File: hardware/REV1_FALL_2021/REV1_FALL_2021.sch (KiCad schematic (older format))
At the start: 23 parts, among them J101 Screw_Terminal_01x02, Q101 Q_NMOS_GDS, U1 Teensy3.6_All_Pins, U2 PA16165_Breakout, U3 MPL3115A2_Breakout, U4 BNO055_Breakout, U5 RFM69HCW_Breakout

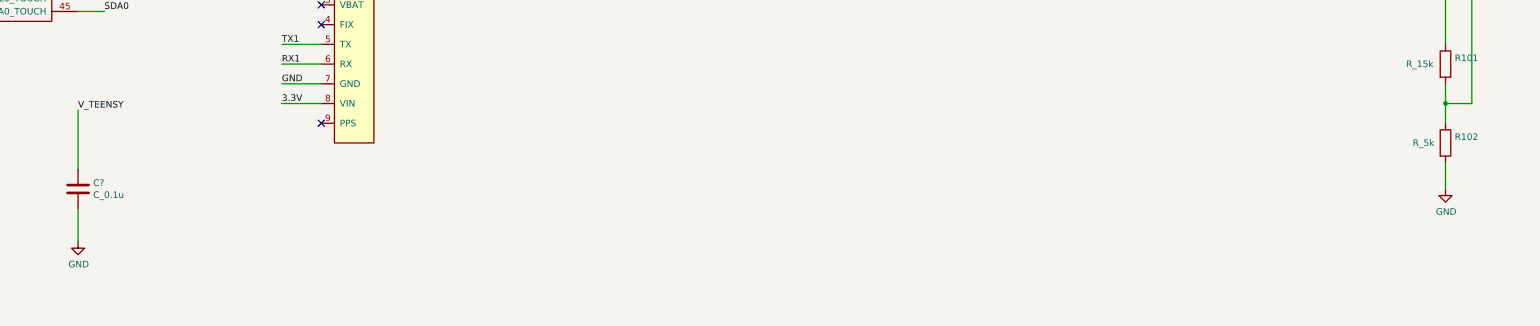
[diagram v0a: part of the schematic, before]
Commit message: change resistance of one voltage divider resistor
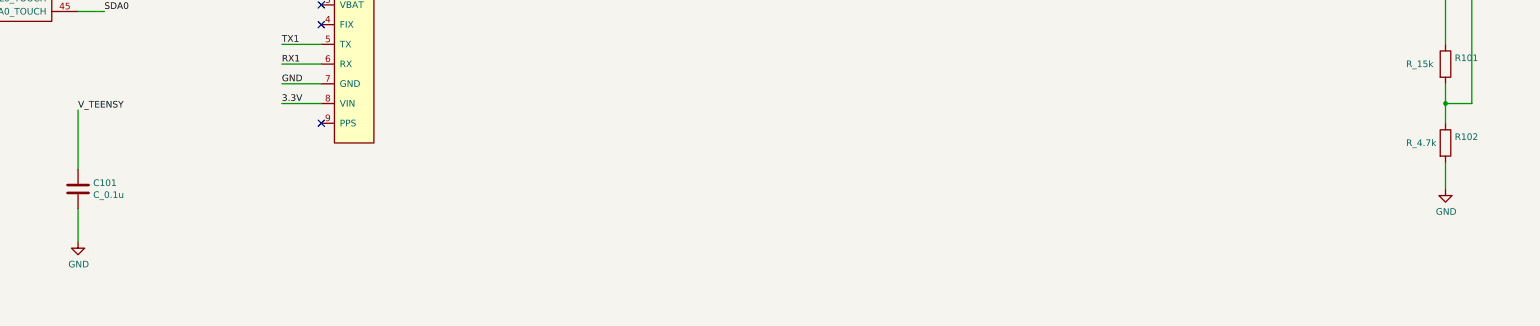
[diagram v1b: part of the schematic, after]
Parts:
- R102: value R_5k -> R_4.7k
- gave numbers to parts that had none: 1
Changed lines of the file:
@@
 P 14150 6750
 F 0 "R102" H 14220 6796 50  0000 L CNN
-F 1 "R_5k" H 13900 6750 50  0000 L CNN
+F 1 "R_4.7k" H 13850 6750 50  0000 L CNN
 F 2 "Resistor_SMD:R_0805_2012Metric_Pad1.20x1.40mm_HandSolder" V 14080 6750 50  0001 C CNN
 F 3 "~" H 14150 6750 50  0001 C CNN
@@
 3.3V
 $Comp
-L Device:C C?
+L Device:C C101
 U 1 1 61A04C38
 P 3750 7100
-F 0 "C?" H 3865 7146 50  0000 L CNN
+F 0 "C101" H 3865 7146 50  0000 L CNN
 F 1 "C_0.1u" H 3865 7055 50  0000 L CNN
 F 2 "Capacitor_SMD:C_0805_2012Metric_Pad1.18x1.45mm_HandSolder" H 3788 6950 50  0001 C CNN
@@
 $EndComp
 $Comp
-L power:GND #PWR?
+L power:GND #PWR0107
 U 1 1 61A05A03
 P 3750 7500
-F 0 "#PWR?" H 3750 7250 50  0001 C CNN
+F 0 "#PWR0107" H 3750 7250 50  0001 C CNN
 F 1 "GND" H 3755 7327 50  0000 C CNN
 F 2 "" H 3750 7500 50  0001 C CNN

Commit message: Add second e-match
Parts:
- added J102: Screw_Terminal_01x02, TerminalBlock:TerminalBlock_bornier-2_P5.08mm, symbol Connector:Screw_Terminal_01x02
- added Q102: Q_NMOS_GDS, footprints:TO-220-3, symbol Device:Q_NMOS_GDS
- added R109: R_10k, Resistor_SMD:R_0805_2012Metric_Pad1.20x1.40mm_HandSolder, symbol Device:R
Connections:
- net GND: now also Q102.3 (S)
- net V_EMATCH: now also J102.1 (Pin_1)
- net E-MATCH_TRIGGER_1: now reaches U1.35 (38_A19_PWM_SDA1)
- net E-MATCH_TRIGGER_1: now also R103.2
- net E-MATCH_TRIGGER renamed E-MATCH_TRIGGER_2
- net E-MATCH_TRIGGER_2: now also R109.2; no longer R103.2
- new net: J102.2 (Pin_2), Q102.2 (D)
- new net: Q102.1 (G), R109.1
- no-connect marks 85 -> 84
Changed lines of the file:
@@
 NoConn ~ 1450 4350
 NoConn ~ 1450 4450
-NoConn ~ 1450 4850
 NoConn ~ 1450 5050
 NoConn ~ 1450 5150
@@
 Text Label 4250 4950 0    50   ~ 0
 V_TEENSY
-Text Label 1350 4950 2    50   ~ 0
-E-MATCH_TRIGGER
+Text Label 1350 4850 2    50   ~ 0
+E-MATCH_TRIGGER_1
 Wire Wire Line
 	1450 4950 1350 4950
@@
 $EndSheet
 Text Label 18750 4400 2    50   ~ 0
-E-MATCH_TRIGGER
+E-MATCH_TRIGGER_1
 $Comp
 L Device:Q_NMOS_GDS Q101
@@
 Text Label 3750 6500 0    50   ~ 0
 V_TEENSY
+Text Label 1350 4950 2    50   ~ 0
+E-MATCH_TRIGGER_2
+Wire Wire Line
+	1350 4850 1450 4850
+Text Label 18750 7900 2    50   ~ 0
+E-MATCH_TRIGGER_2
+Text Notes 19500 7000 0    50   ~ 0
+E-Match in series here
+Text Label 20500 6600 0    50   ~ 0
+V_EMATCH
+Wire Wire Line
+	20500 6950 20500 6600
+Wire Wire Line
+	21000 6950 20500 6950
+Wire Wire Line
+	20500 7050 21000 7050
+$Comp
+L power:GND #PWR0108
+U 1 1 619F16BC
+P 20500 8750
+F 0 "#PWR0108" H 20500 8500 50  0001 C CNN
+F 1 "GND" H 20505 8577 50  0000 C CNN
+F 2 "" H 20500 8750 50  0001 C CNN
+F 3 "" H 20500 8750 50  0001 C CNN
+	1    20500 8750
+	1    0    0    -1
+$EndComp
+Wire Wire Line
+	20500 7700 20500 7050
+Wire Wire Line
+	20500 8750 20500 8100
+$Comp
+L Connector:Screw_Terminal_01x02 J102
+U 1 1 619F16C4
+P 21200 6950
+F 0 "J102" H 21280 6942 50  0000 L CNN
+F 1 "Screw_Terminal_01x02" H 21280 6851 50  0000 L CNN
+F 2 "TerminalBlock:TerminalBlock_bornier-2_P5.08mm" H 21200 6950 50  0001 C CNN
+F 3 "~" H 21200 6950 50  0001 C CNN
+	1    21200 6950
+	1    0    0    -1
+$EndComp
+Wire Wire Line
+	19700 7900 20200 7900
+Wire Wire Line
+	18750 7900 19400 7900
+$Comp
+L Device:R R109
+U 1 1 619F16CC
+P 19550 7900
+F 0 "R109" V 19343 7900 50  0000 C CNN
+F 1 "R_10k" V 19434 7900 50  0000 C CNN
+F 2 "Resistor_SMD:R_0805_2012Metric_Pad1.20x1.40mm_HandSolder" V 19480 7900 50  0001 C CNN
+F 3 "~" H 19550 7900 50  0001 C CNN
+	1    19550 7900
+	0    1    1    0
+$EndComp
+$Comp
+L Device:Q_NMOS_GDS Q102
+U 1 1 619F16D2
+P 20400 7900
+F 0 "Q102" H 20604 7946 50  0000 L CNN
+F 1 "Q_NMOS_GDS" H 20604 7855 50  0000 L CNN
+F 2 "footprints:TO-220-3" H 20600 8000 50  0001 C CNN
+F 3 "~" H 20400 7900 50  0001 C CNN
+	1    20400 7900
+	1    0    0    -1
+$EndComp
 $EndSCHEMATC

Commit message: Change footprint of TPS2113A to the TSSOP package
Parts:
- R101: LCSC (none) -> 0805W8F1502T5E
- R102: LCSC (none) -> 0805W8F4701T5E
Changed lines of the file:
@@
 F 2 "Resistor_SMD:R_0805_2012Metric_Pad1.20x1.40mm_HandSolder" V 14080 6750 50  0001 C CNN
 F 3 "~" H 14150 6750 50  0001 C CNN
+F 4 "0805W8F4701T5E" H 14150 6750 50  0001 C CNN "LCSC"
 	1    14150 6750
 	1    0    0    -1
@@
 F 2 "Resistor_SMD:R_0805_2012Metric_Pad1.20x1.40mm_HandSolder" V 14080 6150 50  0001 C CNN
 F 3 "~" H 14150 6150 50  0001 C CNN
+F 4 "0805W8F1502T5E" H 14150 6150 50  0001 C CNN "LCSC"
 	1    14150 6150
 	1    0    0    -1

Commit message: update all fab-outputs, as ordered
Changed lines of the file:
@@
+	1    0    0    -1
+$EndComp
+$Comp
+L Graphic:Logo_Open_Hardware_Large #LOGO101
+U 1 1 61A018C9
+P 1750 11700
+F 0 "#LOGO101" H 1750 12200 50  0001 C CNN
+F 1 "Logo_Open_Hardware_Large" H 1750 11300 50  0001 C CNN
+F 2 "Olin_Rocketry:Olin_O" H 1750 11700 50  0001 C CNN
+F 3 "~" H 1750 11700 50  0001 C CNN
+	1    1750 11700
+	1    0    0    -1
+$EndComp
+$Comp
+L Graphic:Logo_Open_Hardware_Large #LOGO102
+U 1 1 61A0241D
+P 2900 11700
+F 0 "#LOGO102" H 2900 12200 50  0001 C CNN
+F 1 "Logo_Open_Hardware_Large" H 2900 11300 50  0001 C CNN
+F 2 "Olin_Rocketry:Olin_Rocketry_Logo1" H 2900 11700 50  0001 C CNN
+F 3 "~" H 2900 11700 50  0001 C CNN
+	1    2900 11700
 	1    0    0    -1
 $EndComp

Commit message: add terminals for arming switches
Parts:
- added J? (x2): Screw_Terminal_01x02, symbol Connector:Screw_Terminal_01x02
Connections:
- net V_EMATCH: now also J?.1 (Pin_1)
- net V_TEENSY: now also J?.1 (Pin_1)
- new net TPS2113A for E-match/VOUT: J?.2 (Pin_2)
- new net TPS2113A for Teensy power/VOUT: J?.2 (Pin_2)
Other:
- note added: "Battery 1"
- note added: "Battery 2"
- note added: "Power Multiplexer"
- note added: "Terminals to Electrical \nArming Switch"
- note added: "Terminals to Electromechanical \nArming Switch"
- moved on the sheet: J101, J102, Q101, Q102, R103, R109
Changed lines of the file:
@@
 F 1 "PA16165_Breakout" H 5500 7050 50  0000 L CNN
 F 2 "sensors_2021_2022:PA16165_Breakout" H 5800 6650 50  0001 C CNN
-F 3 "" H 5800 6650 50  0001 C CNN
+F 3 "https://www.adafruit.com/product/746" H 5800 6650 50  0001 C CNN
 	1    5850 6000
 	1    0    0    -1
@@
 Wire Wire Line
 	1450 4950 1350 4950
-Text Notes 19500 3500 0    50   ~ 0
+Text Notes 21250 2950 0    75   ~ 0
 E-Match in series here
-Text Label 20500 3100 0    50   ~ 0
+Text Label 21050 2250 0    50   ~ 0
 V_EMATCH
 Wire Wire Line
-	20500 3450 20500 3100
-Wire Wire Line
-	21000 3450 20500 3450
-Wire Wire Line
-	20500 3550 21000 3550
+	21050 2600 21050 2250
+Wire Wire Line
+	21550 2600 21050 2600
+Wire Wire Line
+	21050 2700 21550 2700
 $Comp
 L power:GND #PWR0112
 U 1 1 61A7D7C2
-P 20500 5250
-F 0 "#PWR0112" H 20500 5000 50  0001 C CNN
-F 1 "GND" H 20505 5077 50  0000 C CNN
-F 2 "" H 20500 5250 50  0001 C CNN
-F 3 "" H 20500 5250 50  0001 C CNN
-	1    20500 5250
-	1    0    0    -1
-$EndComp
-Wire Wire Line
-	20500 4200 20500 3550
-Wire Wire Line
-	20500 5250 20500 4600
+P 21050 4400
+F 0 "#PWR0112" H 21050 4150 50  0001 C CNN
+F 1 "GND" H 21055 4227 50  0000 C CNN
+F 2 "" H 21050 4400 50  0001 C CNN
+F 3 "" H 21050 4400 50  0001 C CNN
+	1    21050 4400
+	1    0    0    -1
+$EndComp
+Wire Wire Line
+	21050 3350 21050 2700
+Wire Wire Line
+	21050 4400 21050 3750
 $Comp
 L Connector:Screw_Terminal_01x02 J101
 U 1 1 61A64E05
-P 21200 3450
-F 0 "J101" H 21280 3442 50  0000 L CNN
-F 1 "Screw_Terminal_01x02" H 21280 3351 50  0000 L CNN
-F 2 "TerminalBlock:TerminalBlock_bornier-2_P5.08mm" H 21200 3450 50  0001 C CNN
-F 3 "~" H 21200 3450 50  0001 C CNN
-	1    21200 3450
-	1    0    0    -1
-$EndComp
-Wire Wire Line
-	19700 4400 20200 4400
-Wire Wire Line
-	18750 4400 19400 4400
+P 21750 2600
+F 0 "J101" H 21830 2592 50  0000 L CNN
+F 1 "Screw_Terminal_01x02" H 21830 2501 50  0000 L CNN
+F 2 "TerminalBlock:TerminalBlock_bornier-2_P5.08mm" H 21750 2600 50  0001 C CNN
+F 3 "~" H 21750 2600 50  0001 C CNN
+	1    21750 2600
+	1    0    0    -1
+$EndComp
+Wire Wire Line
+	20550 3550 20750 3550
+Wire Wire Line
+	19950 3550 20250 3550
 $Comp
 L Device:R R103
 U 1 1 61A5D0C7
-P 19550 4400
-F 0 "R103" V 19343 4400 50  0000 C CNN
-F 1 "R_10k" V 19434 4400 50  0000 C CNN
-F 2 "Resistor_SMD:R_0805_2012Metric_Pad1.20x1.40mm_HandSolder" V 19480 4400 50  0001 C CNN
-F 3 "~" H 19550 4400 50  0001 C CNN
-	1    19550 4400
+P 20400 3550
+F 0 "R103" V 20193 3550 50  0000 C CNN
+F 1 "R_10k" V 20284 3550 50  0000 C CNN
+F 2 "Resistor_SMD:R_0805_2012Metric_Pad1.20x1.40mm_HandSolder" V 20330 3550 50  0001 C CNN
+F 3 "~" H 20400 3550 50  0001 C CNN
+	1    20400 3550
 	0    1    1    0
 $EndComp
-Wire Wire Line
-	16150 5050 16900 5050
-Text Label 16900 5050 0    50   ~ 0
+Text Label 17700 4200 0    50   ~ 0
 V_TEENSY
-Wire Wire Line
-	16900 2700 16100 2700
-Text Label 16900 2700 0    50   ~ 0
+Text Label 17700 2050 0    50   ~ 0
 V_EMATCH
 Wire Wire Line
@@
 Wire Wire Line
 	16150 5400 16900 5400
-Text Label 13500 3050 2    50   ~ 0
+Text Label 15100 3700 0    50   ~ 0
 BALANCE_CONTROL
-Wire Wire Line
-	14700 3050 13500 3050
 $Comp
 L power:GND #PWR0111
@@
 F6 "VSNS" I L 14750 5400 50
 $EndSheet
-Text Label 18750 4400 2    50   ~ 0
+Text Label 19950 3550 2    50   ~ 0
 E-MATCH_TRIGGER_1
 $Comp
 L Device:Q_NMOS_GDS Q101
 U 1 1 619E7B0C
-P 20400 4400
-F 0 "Q101" H 20604 4446 50  0000 L CNN
-F 1 "Q_NMOS_GDS" H 20604 4355 50  0000 L CNN
-F 2 "footprints:TO-220-3" H 20600 4500 50  0001 C CNN
-F 3 "~" H 20400 4400 50  0001 C CNN
-	1    20400 4400
+P 20950 3550
+F 0 "Q101" H 21154 3596 50  0000 L CNN
+F 1 "Q_NMOS_GDS" H 21154 3505 50  0000 L CNN
+F 2 "footprints:TO-220-3" H 21150 3650 50  0001 C CNN
+F 3 "https://www.onsemi.com/pdf/datasheet/tip120-d.pdf" H 20950 3550 50  0001 C CNN
+	1    20950 3550
 	1    0    0    -1
 $EndComp
@@
 Wire Wire Line
 	1350 4850 1450 4850
-Text Label 18750 7900 2    50   ~ 0
+Text Label 19300 6550 2    50   ~ 0
 E-MATCH_TRIGGER_2
-Text Notes 19500 7000 0    50   ~ 0
+Text Notes 21250 5950 0    75   ~ 0
 E-Match in series here
-Text Label 20500 6600 0    50   ~ 0
+Text Label 21050 5250 0    50   ~ 0
 V_EMATCH
 Wire Wire Line
-	20500 6950 20500 6600
-Wire Wire Line
-	21000 6950 20500 6950
-Wire Wire Line
-	20500 7050 21000 7050
+	21050 5600 21050 5250
+Wire Wire Line
+	21550 5600 21050 5600
+Wire Wire Line
+	21050 5700 21550 5700
 $Comp
 L power:GND #PWR0108
 U 1 1 619F16BC
-P 20500 8750
-F 0 "#PWR0108" H 20500 8500 50  0001 C CNN
-F 1 "GND" H 20505 8577 50  0000 C CNN
-F 2 "" H 20500 8750 50  0001 C CNN
-F 3 "" H 20500 8750 50  0001 C CNN
-	1    20500 8750
-	1    0    0    -1
-$EndComp
-Wire Wire Line
-	20500 7700 20500 7050
-Wire Wire Line
-	20500 8750 20500 8100
+P 21050 7400
+F 0 "#PWR0108" H 21050 7150 50  0001 C CNN
+F 1 "GND" H 21055 7227 50  0000 C CNN
+F 2 "" H 21050 7400 50  0001 C CNN
+F 3 "" H 21050 7400 50  0001 C CNN
+	1    21050 7400
+	1    0    0    -1
+$EndComp
+Wire Wire Line
+	21050 6350 21050 5700
+Wire Wire Line
+	21050 7400 21050 6750
 $Comp
 L Connector:Screw_Terminal_01x02 J102
 U 1 1 619F16C4
-P 21200 6950
-F 0 "J102" H 21280 6942 50  0000 L CNN
-F 1 "Screw_Terminal_01x02" H 21280 6851 50  0000 L CNN
-F 2 "TerminalBlock:TerminalBlock_bornier-2_P5.08mm" H 21200 6950 50  0001 C CNN
-F 3 "~" H 21200 6950 50  0001 C CNN
-	1    21200 6950
-	1    0    0    -1
-$EndComp
-Wire Wire Line
-	19700 7900 20200 7900
-Wire Wire Line
-	18750 7900 19400 7900
+P 21750 5600
+F 0 "J102" H 21830 5592 50  0000 L CNN
+F 1 "Screw_Terminal_01x02" H 21830 5501 50  0000 L CNN
+F 2 "TerminalBlock:TerminalBlock_bornier-2_P5.08mm" H 21750 5600 50  0001 C CNN
+F 3 "~" H 21750 5600 50  0001 C CNN
+	1    21750 5600
+	1    0    0    -1
+$EndComp
+Wire Wire Line
+	20250 6550 20750 6550
+Wire Wire Line
+	19300 6550 19950 6550
 $Comp
 L Device:R R109
 U 1 1 619F16CC
-P 19550 7900
-F 0 "R109" V 19343 7900 50  0000 C CNN
-F 1 "R_10k" V 19434 7900 50  0000 C CNN
-F 2 "Resistor_SMD:R_0805_2012Metric_Pad1.20x1.40mm_HandSolder" V 19480 7900 50  0001 C CNN
-F 3 "~" H 19550 7900 50  0001 C CNN
-	1    19550 7900
+P 20100 6550
+F 0 "R109" V 19893 6550 50  0000 C CNN
+F 1 "R_10k" V 19984 6550 50  0000 C CNN
+F 2 "Resistor_SMD:R_0805_2012Metric_Pad1.20x1.40mm_HandSolder" V 20030 6550 50  0001 C CNN
+F 3 "~" H 20100 6550 50  0001 C CNN
+	1    20100 6550
 	0    1    1    0
 $EndComp
@@
 L Device:Q_NMOS_GDS Q102
 U 1 1 619F16D2
-P 20400 7900
-F 0 "Q102" H 20604 7946 50  0000 L CNN
-F 1 "Q_NMOS_GDS" H 20604 7855 50  0000 L CNN
-F 2 "footprints:TO-220-3" H 20600 8000 50  0001 C CNN
-F 3 "~" H 20400 7900 50  0001 C CNN
-	1    20400 7900
-	1    0    0    -1
-$EndComp
-$Comp
-L Graphic:Logo_Open_Hardware_Large #LOGO101
-U 1 1 61A018C9
-P 1750 11700
-F 0 "#LOGO101" H 1750 12200 50  0001 C CNN
-F 1 "Logo_Open_Hardware_Large" H 1750 11300 50  0001 C CNN
-F 2 "Olin_Rocketry:Olin_O" H 1750 11700 50  0001 C CNN
-F 3 "~" H 1750 11700 50  0001 C CNN
-	1    1750 11700
-	1    0    0    -1
-$EndComp
-$Comp
-L Graphic:Logo_Open_Hardware_Large #LOGO102
-U 1 1 61A0241D
-P 2900 11700
-F 0 "#LOGO102" H 2900 12200 50  0001 C CNN
-F 1 "Logo_Open_Hardware_Large" H 2900 11300 50  0001 C CNN
-F 2 "Olin_Rocketry:Olin_Rocketry_Logo1" H 2900 11700 50  0001 C CNN
-F 3 "~" H 2900 11700 50  0001 C CNN
-	1    2900 11700
-	1    0    0    -1
-$EndComp
+P 20950 6550
+F 0 "Q102" H 21154 6596 50  0000 L CNN
+F 1 "Q_NMOS_GDS" H 21154 6505 50  0000 L CNN
+F 2 "footprints:TO-220-3" H 21150 6650 50  0001 C CNN
+F 3 "https://www.onsemi.com/pdf/datasheet/tip120-d.pdf" H 20950 6550 50  0001 C CNN
+	1    20950 6550
+	1    0    0    -1
+$EndComp
+Wire Wire Line
+	14700 3050 14450 3050
+Wire Wire Line
+	14450 3050 14450 3700
+Wire Wire Line
+	14450 3700 15100 3700
+$Comp
+L Connector:Screw_Terminal_01x02 J?
+U 1 1 61BAEBD9
+P 17900 2600
+F 0 "J?" H 17980 2592 50  0000 L CNN
+F 1 "Screw_Terminal_01x02" H 17980 2501 50  0000 L CNN
+F 2 "" H 17900 2600 50  0001 C CNN
+F 3 "~" H 17900 2600 50  0001 C CNN
+	1    17900 2600
+	1    0    0    -1
+$EndComp
+Wire Wire Line
+	16100 2700 17700 2700
+Wire Wire Line
+	17700 2600 17700 2050
+Text Notes 17750 3050 0    75   ~ 0
+Terminals to Electromechanical \nArming Switch
+$Comp
+L Connector:Screw_Terminal_01x02 J?
+U 1 1 61BB7A24
+P 17900 4950
+F 0 "J?" H 17980 4942 50  0000 L CNN
+F 1 "Screw_Terminal_01x02" H 17980 4851 50  0000 L CNN
+F 2 "" H 17900 4950 50  0001 C CNN
+F 3 "~" H 17900 4950 50  0001 C CNN
+	1    17900 4950
+	1    0    0    -1
+$EndComp
+Wire Wire Line
+	16150 5050 17700 5050
+Wire Wire Line
+	17700 4950 17700 4200
+Text Notes 17750 5450 0    75   ~ 0
+Terminals to Electrical \nArming Switch
+Text Notes 14700 2250 0    100  ~ 0
+Power Multiplexer
+Text Notes 14750 4600 0    100  ~ 0
+Power Multiplexer
+Text Notes 12700 3350 0    75   ~ 0
+Battery 2
+Text Notes 12700 4200 0    75   ~ 0
+Battery 1
 $EndSCHEMATC

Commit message: change both VSNS pins on multiplexers to use the same voltage divider
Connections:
- net BALANCE_CONTROL: no longer names the net of U1.34 (37_A18_PWM_SCL1)
- net TPS2113A for Teensy power/VSNS renamed TPS2113A for E-match/VSNS
- no-connect marks 84 -> 85
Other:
- note added: "Pull-up to VDD"
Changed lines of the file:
@@
 Text Label 900  4650 0    50   ~ 0
 TPS_2_STAT
-Text Label 1350 4750 2    50   ~ 0
-BALANCE_CONTROL
 Wire Wire Line
 	1450 4750 1350 4750
@@
 Wire Wire Line
 	16150 5400 16900 5400
-Text Label 15100 3700 0    50   ~ 0
-BALANCE_CONTROL
 $Comp
 L power:GND #PWR0111
@@
 	1    0    0    -1
 $EndComp
-Wire Wire Line
-	14700 3050 14450 3050
-Wire Wire Line
-	14450 3050 14450 3700
-Wire Wire Line
-	14450 3700 15100 3700
 $Comp
 L Connector:Screw_Terminal_01x02 J?
@@
 Text Notes 12700 4200 0    75   ~ 0
 Battery 1
+Text Notes 20500 2950 0    50   ~ 0
+Pull-up to VDD
+Text Notes 20550 5950 0    50   ~ 0
+Pull-up to VDD
+Wire Wire Line
+	14350 5400 14350 3050
+Connection ~ 14350 5400
+Wire Wire Line
+	14350 3050 14700 3050
+NoConn ~ 1350 4750
 $EndSCHEMATC
